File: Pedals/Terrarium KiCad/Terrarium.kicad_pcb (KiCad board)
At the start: 2 copper layers, 59.4 x 73 mm, 46 parts, among them IC1 TL072CP, IC2 LM78L05, SW5 3PDTTOGGLE

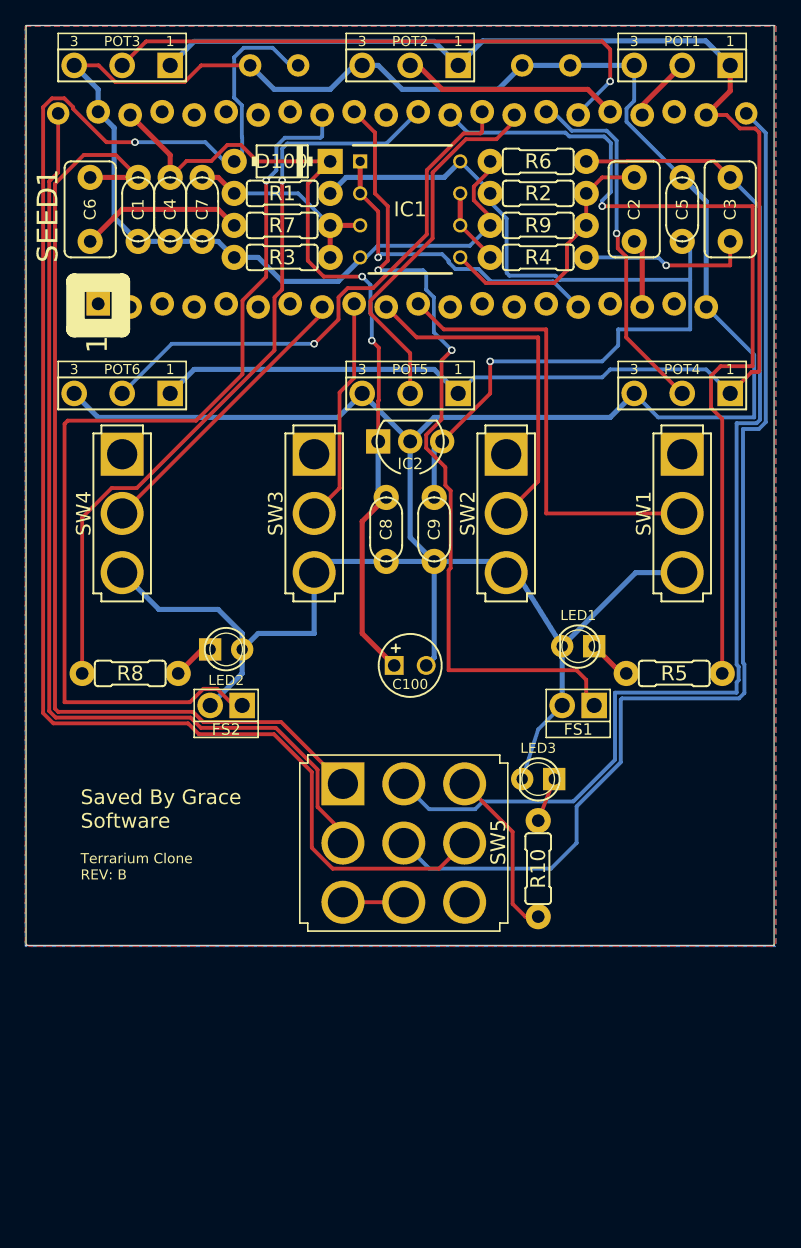
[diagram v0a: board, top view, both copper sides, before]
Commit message: Update board with new components
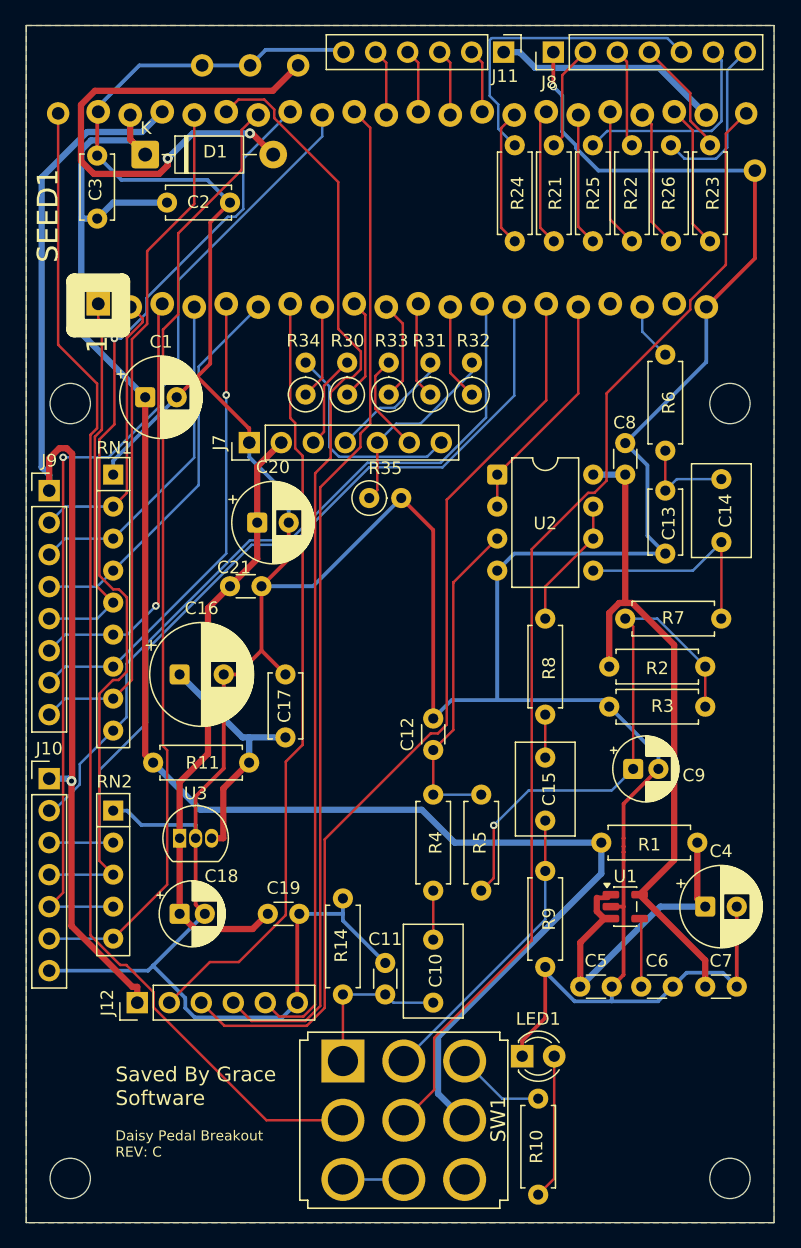
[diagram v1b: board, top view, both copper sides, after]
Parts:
- removed C100: 100u, Terrarium-import-fps:050_2.5MM.2
- removed D100: 1N5817, Terrarium-import-fps:DO41-3
- removed FS1, FS2: SPST, Terrarium-import-fps:SPST
- removed IC1: TL072CP, Terrarium-import-fps:DIP794W53P254L959H508Q8N
- removed IC2: LM78L05, Terrarium-import-fps:TO92-
- removed LED2, LED3: LED.3, Terrarium-import-fps:3MM_2
- removed POT1, POT2, POT3, POT4, POT5, POT6: B10K, Terrarium-import-fps:16MM_PADS.2
- removed the SW1 at (170.9, 107.2)
- removed SW2, SW3, SW4: , Terrarium-import-fps:SPDT_SOLDER_LUG
- added C10: 1uF, Capacitor_THT:C_Rect_L7.2mm_W4.5mm_P5.00mm_FKS2_FKP2_MKS2_MKP2, F.Cu at (151.1, 146.1)
- added C11: 100pF, Capacitor_THT:C_Disc_D3.0mm_W1.6mm_P2.50mm, F.Cu at (147.3, 145.4)
- added C12: 1nF, Capacitor_THT:C_Disc_D3.0mm_W1.6mm_P2.50mm, F.Cu at (151.1, 126.0)
- added C13: 2.2nF, Capacitor_THT:C_Disc_D5.0mm_W2.5mm_P5.00mm, F.Cu at (169.6, 105.4)
- added C14: 1uF, Capacitor_THT:C_Rect_L7.2mm_W4.5mm_P5.00mm_FKS2_FKP2_MKS2_MKP2, F.Cu at (174.0, 104.5)
- added C15: 1uF, Capacitor_THT:C_Rect_L7.2mm_W4.5mm_P5.00mm_FKS2_FKP2_MKS2_MKP2, F.Cu at (160.0, 126.6)
- added C16: 470uF 16V, Capacitor_THT:CP_Radial_D8.0mm_P3.50mm, F.Cu at (131.0, 120.0)
- added C17: 330nF, Capacitor_THT:C_Disc_D5.0mm_W2.5mm_P5.00mm, F.Cu at (139.4, 125.0)
- added C18: 10uF 16V, Capacitor_THT:CP_Radial_D5.0mm_P2.00mm, F.Cu at (131.0, 139.0)
- added C19: 100nF, Capacitor_THT:C_Disc_D3.0mm_W1.6mm_P2.50mm, F.Cu at (138.0, 139.0)
- added C20: 100uF 16V, Capacitor_THT:CP_Radial_D6.3mm_P2.50mm, F.Cu at (137.2, 108.0)
- added C21: 100nF, Capacitor_THT:C_Disc_D3.0mm_W1.6mm_P2.50mm, F.Cu at (135.0, 113.0)
- added D1: 1N5817, Diode_THT:D_DO-41_SOD81_P10.16mm_Horizontal, F.Cu at (128.3, 78.7)
- added H1: M3, MountingHole:MountingHole_3.2mm_M3, F.Cu at (122.3, 98.5)
- added H2: M3, MountingHole:MountingHole_3.2mm_M3, F.Cu at (174.7, 98.5)
- added H3: M3, MountingHole:MountingHole_3.2mm_M3, F.Cu at (122.3, 160.0)
- added H4: M3, MountingHole:MountingHole_3.2mm_M3, F.Cu at (174.7, 160.0)
- added J10: SPDT + encoder, Connector_PinHeader_2.54mm:PinHeader_1x07_P2.54mm_Vertical, F.Cu at (120.7, 128.3)
- added J11: Pots, Connector_PinHeader_2.54mm:PinHeader_1x06_P2.54mm_Vertical, F.Cu at (156.7, 70.6)
- added J12: Spare GPIO, Connector_PinHeader_2.54mm:PinHeader_1x06_P2.54mm_Vertical, F.Cu at (127.6, 146.1)
- added J7: OLED SPI, Connector_PinHeader_2.54mm:PinHeader_1x07_P2.54mm_Vertical, F.Cu at (136.5, 101.6)
- added J8: LEDs, Connector_PinHeader_2.54mm:PinHeader_1x07_P2.54mm_Vertical, F.Cu at (160.7, 70.6)
- added J9: FX switches + tap, Connector_PinHeader_2.54mm:PinHeader_1x08_P2.54mm_Vertical, F.Cu at (120.7, 105.4)
- added R11: 10R, Resistor_THT:R_Axial_DIN0207_L6.3mm_D2.5mm_P7.62mm_Horizontal, F.Cu at (128.9, 127.0)
- added R14: 1M, Resistor_THT:R_Axial_DIN0207_L6.3mm_D2.5mm_P7.62mm_Horizontal, F.Cu at (144.0, 145.4)
- added R21: 2.2k, Resistor_THT:R_Axial_DIN0207_L6.3mm_D2.5mm_P7.62mm_Horizontal, F.Cu at (160.7, 85.6)
- added R22: 2.2k, Resistor_THT:R_Axial_DIN0207_L6.3mm_D2.5mm_P7.62mm_Horizontal, F.Cu at (166.9, 85.6)
- added R23: 2.2k, Resistor_THT:R_Axial_DIN0207_L6.3mm_D2.5mm_P7.62mm_Horizontal, F.Cu at (173.1, 85.6)
- added R24: 2.2k, Resistor_THT:R_Axial_DIN0207_L6.3mm_D2.5mm_P7.62mm_Horizontal, F.Cu at (157.6, 85.6)
- added R25: 2.2k, Resistor_THT:R_Axial_DIN0207_L6.3mm_D2.5mm_P7.62mm_Horizontal, F.Cu at (163.8, 85.6)
- added R26: 2.2k, Resistor_THT:R_Axial_DIN0207_L6.3mm_D2.5mm_P7.62mm_Horizontal, F.Cu at (170.0, 85.6)
- added R30: 47R, Resistor_THT:R_Axial_DIN0207_L6.3mm_D2.5mm_P2.54mm_Vertical, F.Cu at (144.3, 97.8)
- added R31: 47R, Resistor_THT:R_Axial_DIN0207_L6.3mm_D2.5mm_P2.54mm_Vertical, F.Cu at (150.9, 97.8)
- added R32: 47R, Resistor_THT:R_Axial_DIN0207_L6.3mm_D2.5mm_P2.54mm_Vertical, F.Cu at (154.2, 97.8)
- added R33: 47R, Resistor_THT:R_Axial_DIN0207_L6.3mm_D2.5mm_P2.54mm_Vertical, F.Cu at (147.6, 97.8)
- added R34: 47R, Resistor_THT:R_Axial_DIN0207_L6.3mm_D2.5mm_P2.54mm_Vertical, F.Cu at (141.0, 97.8)
- added R35: 10k, Resistor_THT:R_Axial_DIN0207_L6.3mm_D2.5mm_P2.54mm_Vertical, F.Cu at (146.1, 106.0)
- added RN1: 10k, Resistor_THT:R_Array_SIP9, F.Cu at (125.7, 104.1)
- added RN2: 10k, Resistor_THT:R_Array_SIP5, F.Cu at (125.7, 130.8)
- added U1: LP2985-5.0, Package_TO_SOT_SMD:SOT-23-5, F.Cu at (166.4, 138.4)
- added U2: MCP6022, Package_DIP:DIP-8_W7.62mm, F.Cu at (156.2, 104.1)
- added U3: 78L05, Package_TO_SOT_THT:TO-92_Inline, F.Cu at (131.0, 133.0)
- C1: value 100p -> 100uF 16V; footprint Terrarium-import-fps:5MM -> Capacitor_THT:CP_Radial_D6.3mm_P2.50mm
- C2, C3: value 1u -> 100nF; footprint Terrarium-import-fps:.33UF+ -> Capacitor_THT:C_Disc_D5.0mm_W2.5mm_P5.00mm
- C4: value 100n -> 100uF 16V; footprint Terrarium-import-fps:5MM -> Capacitor_THT:CP_Radial_D6.3mm_P2.50mm
- C5: value 100n -> 1uF; footprint Terrarium-import-fps:5MM -> Capacitor_THT:C_Disc_D3.0mm_W1.6mm_P2.50mm
- C6: value 1u -> 10nF; footprint Terrarium-import-fps:.33UF+ -> Capacitor_THT:C_Disc_D3.0mm_W1.6mm_P2.50mm
- C7: value 1n -> 4.7uF; footprint Terrarium-import-fps:5MM -> Capacitor_THT:C_Disc_D3.0mm_W1.6mm_P2.50mm
- C8: value 100n -> 100nF; footprint Terrarium-import-fps:5MM -> Capacitor_THT:C_Disc_D3.0mm_W1.6mm_P2.50mm
- C9: value 100n -> 47uF 16V; footprint Terrarium-import-fps:5MM -> Capacitor_THT:CP_Radial_D5.0mm_P2.00mm
- GND1: renamed from GND0; value PADRD -> GND
- IN1: renamed from IN0; value PADRD -> IN
- INGND1: renamed from IN_GND0; value PADRD -> IN GND
- LED1: value LED.3 -> LED 3mm; footprint Terrarium-import-fps:3MM_2 -> LED_THT:LED_D3.0mm
- OUT1: renamed from OUT0; value PADRD -> OUT
- OUTGND1: renamed from OUT_GND0; value PADRD -> OUT GND
- PWR1: renamed from PWR0; value PADRD -> 9V
- R1: value 1M -> 10R; footprint Terrarium-import-fps:7.5MM.2 -> Resistor_THT:R_Axial_DIN0207_L6.3mm_D2.5mm_P7.62mm_Horizontal
- R10: value 4.7K -> 4.7k; footprint Terrarium-import-fps:7.5MM.2 -> Resistor_THT:R_Axial_DIN0207_L6.3mm_D2.5mm_P7.62mm_Horizontal
- R2, R3, R9: value 1M -> 100k; footprint Terrarium-import-fps:7.5MM.2 -> Resistor_THT:R_Axial_DIN0207_L6.3mm_D2.5mm_P7.62mm_Horizontal
- R4: value 100R -> 1k; footprint Terrarium-import-fps:7.5MM.2 -> Resistor_THT:R_Axial_DIN0207_L6.3mm_D2.5mm_P7.62mm_Horizontal
- R5, R7: value 1K -> 1M; footprint Terrarium-import-fps:7.5MM.2 -> Resistor_THT:R_Axial_DIN0207_L6.3mm_D2.5mm_P7.62mm_Horizontal
- R6: value 100K -> 3.3k; footprint Terrarium-import-fps:7.5MM.2 -> Resistor_THT:R_Axial_DIN0207_L6.3mm_D2.5mm_P7.62mm_Horizontal
- R8: value 1K -> 100R; footprint Terrarium-import-fps:7.5MM.2 -> Resistor_THT:R_Axial_DIN0207_L6.3mm_D2.5mm_P7.62mm_Horizontal
- SEED1: value ES_DAISY_SEED -> Daisy Seed / Seed3
- SW1: renamed from SW5; value 3PDTTOGGLE -> 3PDT
- moved C6 75.6 mm to (167.6, 144.8), turned to 0 degrees
- moved C7 73.5 mm to (172.7, 144.8), turned to 0 degrees
- moved C4 69.8 mm to (172.7, 138.4), turned to 0 degrees
- moved C5 62.2 mm to (162.8, 144.8), turned to 0 degrees
- moved R1 57.4 mm to (164.5, 133.3), turned to 0 degrees
- moved R9 51.2 mm to (160.0, 135.6), turned to -90 degrees
- moved R4 50.9 mm to (151.1, 137.2), turned to 90 degrees
- moved C3 50.2 mm to (124.5, 83.8)
- moved R3 49.0 mm to (172.7, 122.6)
- moved R7 41.4 mm to (166.4, 115.6), turned to 0 degrees
- moved R2 38.0 mm to (165.1, 119.4), turned to 0 degrees
- moved C2 37.1 mm to (130.0, 82.5), turned to 0 degrees
- moved R8 33.2 mm to (160.0, 115.6), turned to -90 degrees
- moved LED1 32.8 mm to (158.2, 150.3), turned to 0 degrees
- moved GND1 25.4 mm to (132.8, 71.7)
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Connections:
- net BYPASS renamed /BYPASS
- net N$13 renamed /JACK_IN
- net N$19 renamed /BYP_LED_R
- net N$21 renamed /JACK_OUT
- C1 pad 1: GND -> /+9V
- C1 pad 2: N$12 -> /GND
- C2 pad 1: LEFT_OUT -> /+9V
- C2 pad 2: N$17 -> /GND
- C3 pad 1: N$10 -> /+9V
- C3 pad 2: N$11 -> /GND
- C4 pad 1: VCC -> /+9V_A
- C4 pad 2: GND -> /GND
- C5 pad 1: +5V -> /+9V_A
- C5 pad 2: GND -> /GND
- C6 pad 1: N$12 -> /LDO_BP
- C6 pad 2: N$15 -> /GND
- C7 pad 1: GND -> /+5V_A
- C7 pad 2: N$16 -> /GND
- C8 pad 1: VCC -> /+5V_A
- C8 pad 2: GND -> /GND
- C9 pad 1: +5V -> /VBIAS
- C9 pad 2: GND -> /GND
- GND1 pad P$1: GND -> /GND
- INGND1 pad P$1: GND -> /GND
- OUTGND1 pad P$1: GND -> /GND
- PWR1 pad P$1: N$9 -> /9V_IN
- R1 pad 1: +5V -> /+9V
- R1 pad 2: N$16 -> /+9V_A
- R10 pad 2: N$20 -> /BYP_LED_A
- R2 pad 1: N$17 -> /+5V_A
- R2 pad 2: +5V -> /VBIAS
- R3 pad 1: N$16 -> /VBIAS
- R3 pad 2: GND -> /GND
- R4 pad 1: N$10 -> /IN_AC
- R4 pad 2: N$14 -> /IN_BUF
- R5 pad 1: N$7 -> /VBIAS
- R5 pad 2: LED1 -> /IN_BUF
- R6 pad 1: N$11 -> /SEED_OUT_L
- R6 pad 2: GND -> /OUT_LPF
- R7 pad 1: N$16 -> /VBIAS
- R7 pad 2: N$15 -> /OUT_BUF
- R8 pad 1: N$8 -> /OUT_DRV
- R8 pad 2: LED2 -> /OUT_R
- R9 pad 1: GND -> /OUT_FX
- R9 pad 2: N$17 -> /GND
- SEED1 pad 1: (no net) -> /FX4
- SEED1 pad 10: SW2 -> /OLED_DC
- SEED1 pad 11: SW1 -> /OLED_MOSI
- SEED1 pad 12: (no net) -> /OLED_RES
- SEED1 pad 13: (no net) -> /SPDT_A
- SEED1 pad 14: (no net) -> /SPDT_B
- SEED1 pad 15: (no net) -> /EXT_D14
- SEED1 pad 16: LEFT_IN -> /SEED_IN_L
- SEED1 pad 17: (no net) -> unconnected-(SEED1-AUDIO_IN_R-Pad17)
- SEED1 pad 18: LEFT_OUT -> /SEED_OUT_L
- SEED1 pad 19: (no net) -> unconnected-(SEED1-AUDIO_OUT_R-Pad19)
- SEED1 pad 2: (no net) -> /FX1
- SEED1 pad 20: GND -> /GND
- SEED1 pad 21: 3V3_A -> /+3V3_A
- SEED1 pad 22: (no net) -> /FXLED3
- SEED1 pad 23: N$1 -> /FXLED6
- SEED1 pad 24: N$2 -> /FXLED2
- SEED1 pad 25: N$3 -> /FXLED5
- SEED1 pad 26: N$4 -> /FXLED1
- SEED1 pad 27: N$5 -> /FXLED4
- SEED1 pad 28: N$6 -> /POT1
- SEED1 pad 29: LED1 -> /POT2
- SEED1 pad 3: (no net) -> /FX5
- SEED1 pad 30: LED2 -> /POT3
- SEED1 pad 31: (no net) -> /POT4
- SEED1 pad 32: FS1 -> /EXT_D25
- SEED1 pad 33: FS2 -> /ENC_B
- SEED1 pad 34: (no net) -> /ENC_A
- SEED1 pad 35: (no net) -> /ENC_SW
- SEED1 pad 36: (no net) -> /EXT_D29
- SEED1 pad 37: (no net) -> /TAP
- SEED1 pad 38: 3V3_D -> /+3V3_D
- SEED1 pad 39: VCC -> /+9V
- SEED1 pad 4: (no net) -> /FX2
- SEED1 pad 40: GND -> /GND
- SEED1 pad 5: (no net) -> /FX6
- SEED1 pad 6: (no net) -> /FX3
- SEED1 pad 7: (no net) -> /EXT_D6
- SEED1 pad 8: SW4 -> /OLED_CS
- SEED1 pad 9: SW3 -> /OLED_SCK
- SW1 pad A1: N$12 -> /IN_FX
- SW1 pad B1: N$11 -> /OUT_FX
- SW1 pad C2: N$9 -> /+9V
- SW1 pad C3: (no net) -> unconnected-(SW1-3-PadC3)
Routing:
- net /GND: track 0.00 -> 359.2 mm, vias 0 -> 1
- net GND: track 289.3 -> 0.00 mm
- net /+9V: track 0.00 -> 134.3 mm
- net 3V3_A: track 126.7 -> 0.00 mm
- net N$9: track 123.4 -> 0.00 mm, vias 1 -> 0
- net N$11: track 89.9 -> 0.00 mm
- net /+3V3_D: track 0.00 -> 89.6 mm, vias 0 -> 1
- net /EXT_D29: track 0.00 -> 85.1 mm
- net /EXT_D25: track 0.00 -> 81.1 mm
- net N$12: track 79.1 -> 0.00 mm
- net /ENC_B: track 0.00 -> 79.0 mm, vias 0 -> 1
- net FS2: track 77.8 -> 0.00 mm, vias 1 -> 0
- net /ENC_SW: track 0.00 -> 75.6 mm
- net /ENC_A: track 0.00 -> 75.4 mm, vias 0 -> 1
- net /EXT_D14: track 0.00 -> 74.6 mm
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- added copper zone on B.Cu, net /GND
- added copper zone on F.Cu, net /GND
- removed copper zone on B.Cu, net GND
- removed copper zone on F.Cu, net GND
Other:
- board size 59.4 x 73 mm -> 59.4 x 95 mm
- board text added: "Daisy Pedal Breakout REV: C"
- board text removed: "Terrarium Clone REV: B"

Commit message: Final base board changes
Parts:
- removed LED1: LED 3mm, LED_THT:LED_D3.0mm
- added J13: Bypass LED, Connector_PinHeader_2.54mm:PinHeader_1x02_P2.54mm_Vertical, B.Cu at (159.5, 150.3)
- SW1: moved to B.Cu
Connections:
- SW1 pad A1: /IN_FX -> /BYPASS
- SW1 pad A3: /BYPASS -> /IN_FX
- SW1 pad B1: /OUT_FX -> /BYPASS
- SW1 pad B3: /BYPASS -> /OUT_FX
- SW1 pad C1: /BYP_LED_R -> unconnected-(SW1-1-PadC1)
- SW1 pad C3: unconnected-(SW1-3-PadC3) -> /BYP_LED_R
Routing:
- net /GND: track 359.2 -> 358.7 mm, vias 1 -> 89
- net /BYP_LED_A: track 11.5 -> 12.0 mm
